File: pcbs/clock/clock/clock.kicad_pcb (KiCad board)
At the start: 2 copper layers, 89 parts, among them J1 USB_B_Micro, Q1 BSS138, Q10 BSS138, Q11 BSS138, Q12 BSS138, Q2 BSS138, Q3 BSS138, Q4 BSS138, Q5 BSS138, Q6 BSS138, Q7 BSS138, Q8 BSS138, Q9 BSS138, SW1 SW_Push, U1 USBLC6-2SC6, U10 KCSC02-105, U11 KCSC02-105, U12 KCSC02-105, U13 KCSC02-105, U14 KCSC02-105, U15 KCSC02-105, U16 KCSC02-105, U2 AP2112K-3.3, U3 SAMD21Exx, U4 PCF85263ATT, U5 TCA6416APWR, U6 AT24CS01-SSHM, U7 KCSC02-105, U8 KCSC02-105, U9 KCSC02-105, Y1 32.768k

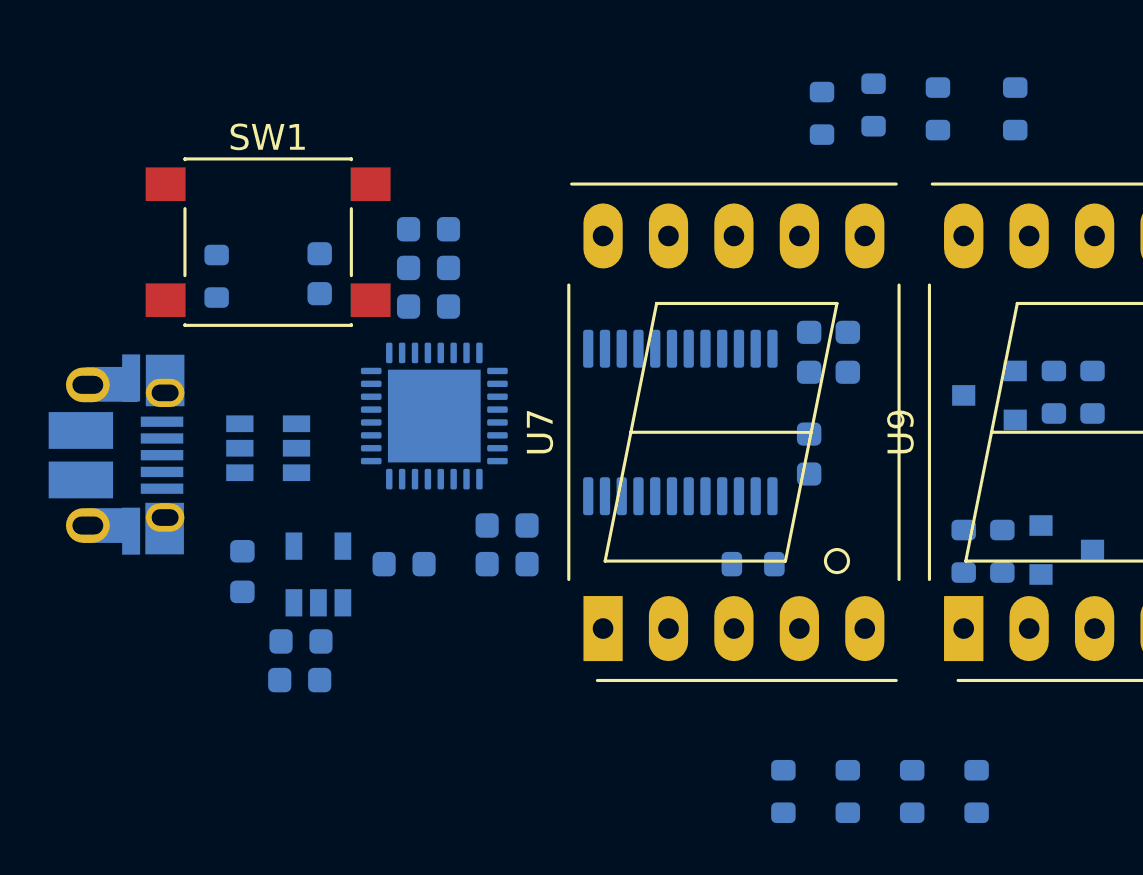
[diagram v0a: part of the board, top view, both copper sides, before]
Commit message: Start clock layout
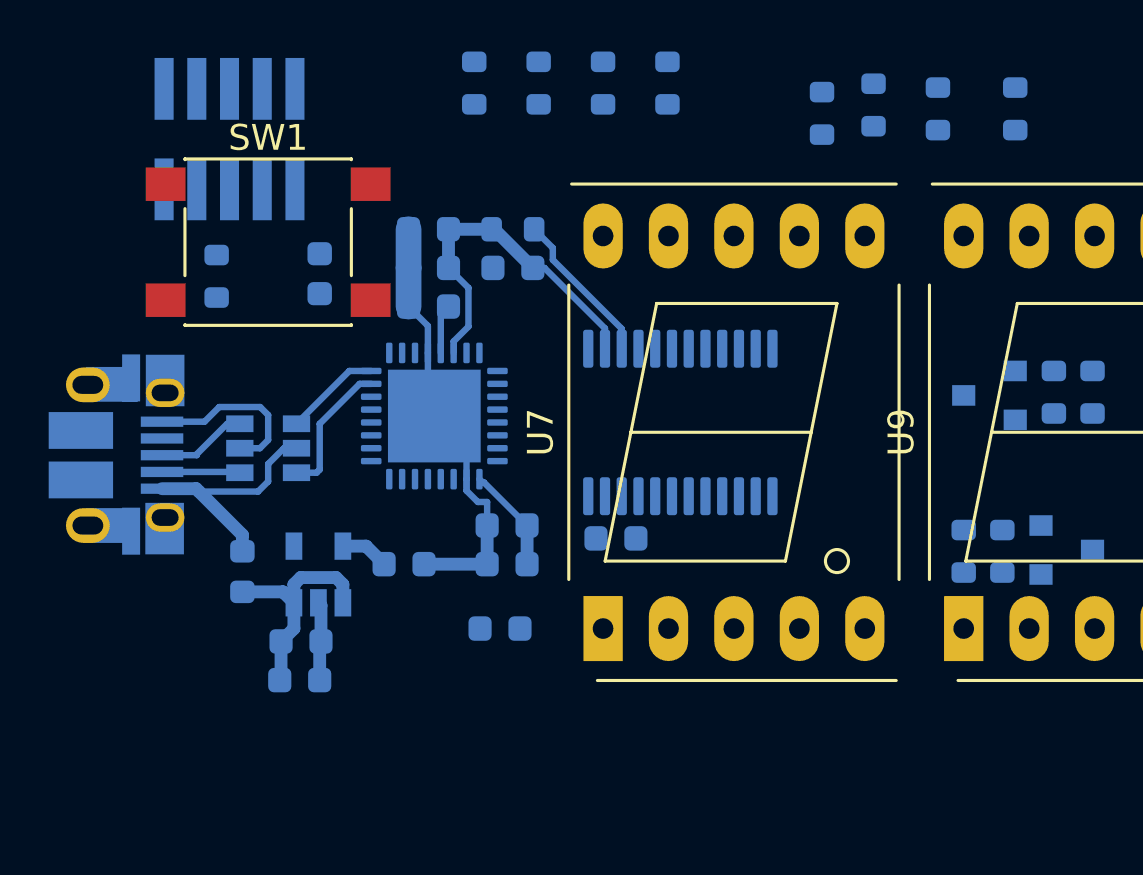
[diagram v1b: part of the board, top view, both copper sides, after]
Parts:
- added J2: CORTEX, Connector_PinHeader_1.27mm:PinHeader_2x05_P1.27mm_Vertical_SMD, B.Cu at (62.5, 116.0)
- moved R11 30.0 mm to (77.0, 113.8)
- moved R12 30.0 mm to (79.5, 113.8)
- moved R13 30.0 mm to (74.5, 113.8)
- moved R16 30.0 mm to (72.0, 113.8)
- moved C12 17.2 mm to (73.0, 135.0), turned to 180 degrees
- moved R8 16.0 mm to (73.5, 119.5), turned to 0 degrees
- moved C11 13.6 mm to (73.5, 121.0), turned to 180 degrees
- moved C13 10.4 mm to (77.5, 131.5), turned to 0 degrees
- turned U5 to 270 degrees
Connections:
- U3 pad 18: /CH6 -> Net-(U3-Pad18)
- U3 pad 19: /CH7 -> Net-(U3-Pad19)
- U3 pad 20: /CH8 -> Net-(U3-Pad20)
- U3 pad 21: /CH9 -> Net-(U3-Pad21)
- U3 pad 22: /CH10 -> Net-(U3-Pad22)
- U3 pad 4: Net-(U3-Pad4) -> /CH6
- U3 pad 5: Net-(U3-Pad5) -> /CH7
- U3 pad 6: Net-(U3-Pad6) -> /CH8
- U3 pad 7: Net-(U3-Pad7) -> /CH9
- U3 pad 8: Net-(U3-Pad8) -> /CH10
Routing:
- net GND: track 0.00 -> 26.7 mm
- net +3V3: track 0.00 -> 19.8 mm
- net Net-(FB1-Pad2): track 0.00 -> 9.38 mm
- net +5V: track 0.00 -> 8.95 mm
- net Net-(R8-Pad2): track 0.00 -> 6.05 mm
- net /USB_N: track 0.00 -> 5.37 mm
- net /USB_P: track 0.00 -> 3.75 mm
- net Net-(J1-Pad3): track 0.00 -> 3.55 mm
- net Net-(J1-Pad2): track 0.00 -> 3.03 mm
- net Net-(C9-Pad2): track 0.00 -> 1.92 mm

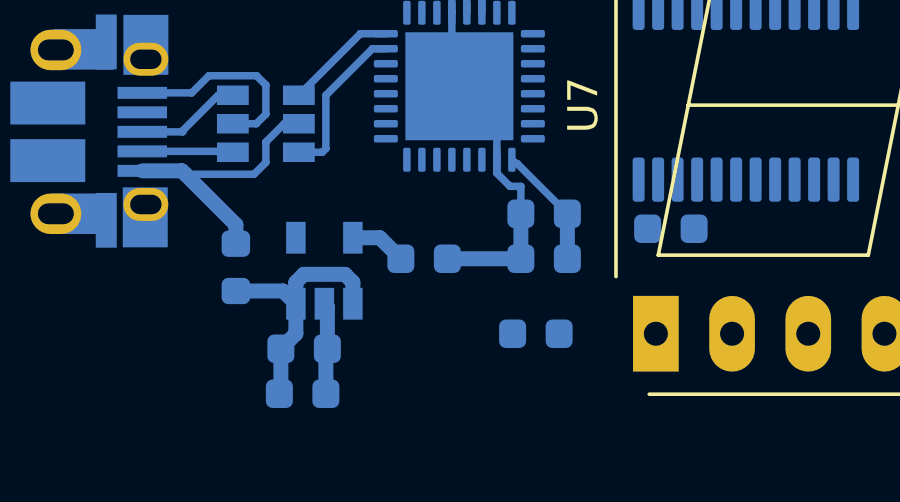
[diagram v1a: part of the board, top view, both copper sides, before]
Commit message: Start clock layout
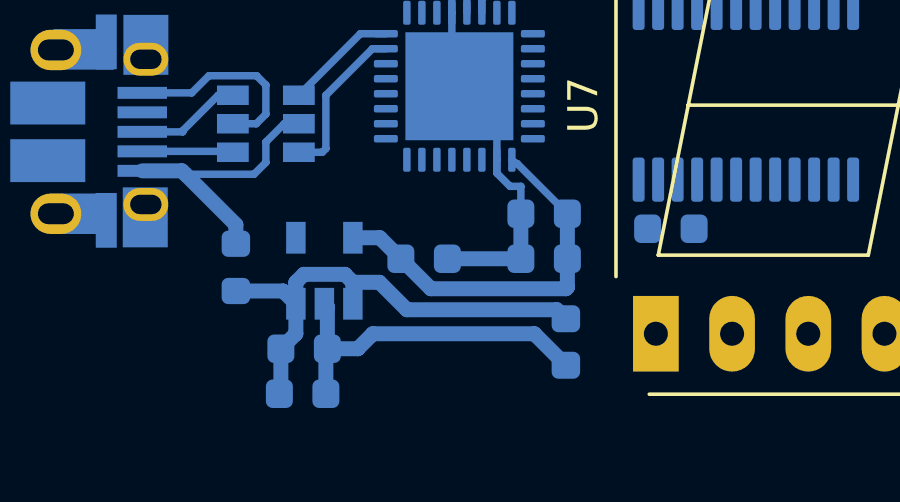
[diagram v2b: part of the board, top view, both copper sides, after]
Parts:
- moved C12 1.04 mm to (74.0, 135.3), turned to 270 degrees
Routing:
- net GND: track 26.7 -> 35.3 mm
- net +5V: track 8.95 -> 16.6 mm
- net +3V3: track 19.8 -> 26.7 mm
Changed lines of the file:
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@@
     (thickness 1.6)
     (drawings 0)
-    (tracks 81)
+    (tracks 93)
     (zones 0)
     (modules 90)
@@
   )
   (module Capacitor_SMD:C_0603_1608Metric (layer B.Cu)
-    (at 73 135 180)
+    (at 74 135.275 270)
     (descr "Capacitor SMD 0603 (1608 Metric), square (rectangular) end terminal, IPC_7351 nominal, (Body size source: IPC-SM-782 page 76, https://www.pcb-3d.com/wordpress/wp-content/uploads/ipc-sm-782a_amendment_1_and_2.pdf), generated with kicad-footprint-generator")
     (tags capacitor)
     (attr smd)
-    (fp_text reference C12 (at 0 1.43) (layer B.SilkS)
+    (fp_text reference C12 (at 0 1.43 90) (layer B.SilkS)
       (effects (font (size 1 1) (thickness 0.15)) (justify mirror))
     )
-    (fp_text value 10u (at 0 -1.43) (layer B.Fab)
+    (fp_text value 10u (at 0 -1.43 90) (layer B.Fab)
       (effects (font (size 1 1) (thickness 0.15)) (justify mirror))
     )
-    (fp_text user %R (at 0 0) (layer B.Fab)
+    (fp_text user %R (at 0 0 90) (layer B.Fab)
       (effects (font (size 0.4 0.4) (thickness 0.06)) (justify mirror))
     )
@@
     (fp_line (start 1.48 0.73) (end 1.48 -0.73) (layer B.CrtYd) (width 0.05))
     (fp_line (start 1.48 -0.73) (end -1.48 -0.73) (layer B.CrtYd) (width 0.05))
-    (pad 2 smd roundrect (at 0.775 0 180) (size 0.9 0.95) (layers B.Cu B.Paste B.Mask) (roundrect_rratio 0.25)
+    (pad 2 smd roundrect (at 0.775 0 270) (size 0.9 0.95) (layers B.Cu B.Paste B.Mask) (roundrect_rratio 0.25)
       (net 2 GND))
-    (pad 1 smd roundrect (at -0.775 0 180) (size 0.9 0.95) (layers B.Cu B.Paste B.Mask) (roundrect_rratio 0.25)
+    (pad 1 smd roundrect (at -0.775 0 270) (size 0.9 0.95) (layers B.Cu B.Paste B.Mask) (roundrect_rratio 0.25)
       (net 5 +5V))
     (model ${KISYS3DMOD}/Capacitor_SMD.3dshapes/C_0603_1608Metric.wrl
@@
   (segment (start 72.5 131) (end 72.5 132.5) (width 0.5) (layer B.Cu) (net 2))
   (segment (start 70.05 132.5) (end 72.5 132.5) (width 0.5) (layer B.Cu) (net 2))
+  (segment (start 72.95 135) (end 74 136.05) (width 0.5) (layer B.Cu) (net 2))
+  (segment (start 67.565002 135) (end 72.95 135) (width 0.5) (layer B.Cu) (net 2))
+  (segment (start 67.065002 135.5) (end 67.565002 135) (width 0.5) (layer B.Cu) (net 2))
+  (segment (start 66.05 135.5) (end 67.065002 135.5) (width 0.5) (layer B.Cu) (net 2))
   (segment (start 71.77501 123.276968) (end 71.77501 121.77501) (width 0.25) (layer B.Cu) (net 3))
   (segment (start 71.77501 121.77501) (end 71 121) (width 0.25) (layer B.Cu) (net 3))
@@
   (segment (start 67.8 131.8) (end 68.5 132.5) (width 0.5) (layer B.Cu) (net 3))
   (segment (start 66.9 131.8) (end 67.8 131.8) (width 0.5) (layer B.Cu) (net 3))
+  (segment (start 74.05 132.5) (end 74.05 133.45) (width 0.5) (layer B.Cu) (net 3))
+  (segment (start 74.05 133.45) (end 74 133.5) (width 0.5) (layer B.Cu) (net 3))
+  (segment (start 69.5 133.5) (end 68.5 132.5) (width 0.5) (layer B.Cu) (net 3))
+  (segment (start 74 133.5) (end 69.5 133.5) (width 0.5) (layer B.Cu) (net 3))
   (segment (start 64.575 133.575) (end 65 134) (width 0.5) (layer B.Cu) (net 5))
   (segment (start 63 133.575) (end 64.575 133.575) (width 0.5) (layer B.Cu) (net 5))
@@
   (segment (start 65 133.284998) (end 65.264999 133.019999) (width 0.5) (layer B.Cu) (net 5))
   (segment (start 65 134) (end 65 133.284998) (width 0.5) (layer B.Cu) (net 5))
+  (segment (start 66.9 133.284998) (end 67.784998 133.284998) (width 0.5) (layer B.Cu) (net 5))
+  (segment (start 67.784998 133.284998) (end 68.70001 134.20001) (width 0.5) (layer B.Cu) (net 5))
+  (segment (start 73.70001 134.20001) (end 74 134.5) (width 0.5) (layer B.Cu) (net 5))
+  (segment (start 68.70001 134.20001) (end 73.70001 134.20001) (width 0.5) (layer B.Cu) (net 5))
   (segment (start 70.7 122.8) (end 71 122.5) (width 0.25) (layer B.Cu) (net 6))
   (segment (start 70.7 124.3) (end 70.7 122.8) (width 0.25) (layer B.Cu) (net 6))

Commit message: Progress
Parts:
- moved C10 133.5 mm to (98.1, 128.7), turned to 180 degrees
- moved U4 129.5 mm to (99.7, 131.2), turned to 180 degrees
- moved Y1 124.4 mm to (104.6, 129.7), turned to 270 degrees
- moved R16 28.2 mm to (86.6, 138.0), turned to 180 degrees
- moved R11 25.0 mm to (83.4, 138.0), turned to 180 degrees
- moved R13 24.3 mm to (77.0, 138.0), turned to 0 degrees
- moved R12 24.2 mm to (80.2, 138.0), turned to 0 degrees
- moved R37 20.0 mm to (94.2, 123.6), turned to 270 degrees
- moved R38 19.2 mm to (95.0, 127.6), turned to 90 degrees
- moved C14 13.9 mm to (95.6, 123.6)
- moved R15 13.1 mm to (77.0, 116.8), turned to 180 degrees
- moved R27 11.3 mm to (106.4, 124.3), turned to 270 degrees
- moved R9 9.83 mm to (83.4, 116.8), turned to 180 degrees
- moved R25 9.11 mm to (104.9, 124.3), turned to 90 degrees
- moved Q7 7.77 mm to (108.9, 124.3), turned to 0 degrees
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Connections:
- U3 pad 13: /CH1 -> /CH6
- U3 pad 14: /CH2 -> /CH7
- U3 pad 15: /CH3 -> /CH8
- U3 pad 16: /CH4 -> /CH9
- U3 pad 17: /CH5 -> /CH10
- U3 pad 4: /CH6 -> /CH1
- U3 pad 5: /CH7 -> /CH2
- U3 pad 6: /CH8 -> /CH3
- U3 pad 7: /CH9 -> /CH4
- U3 pad 8: /CH10 -> /CH5
- U5 pad 10: /Displays/SEG_G -> Net-(U5-Pad10)
- U5 pad 11: /Displays/SEG_DP -> Net-(U5-Pad11)
- U5 pad 17: Net-(U5-Pad17) -> /Displays/SEG_DP
- U5 pad 18: Net-(U5-Pad18) -> /Displays/SEG_C
- U5 pad 19: Net-(U5-Pad19) -> /Displays/SEG_D
- U5 pad 20: Net-(U5-Pad20) -> /Displays/SEG_E
- U5 pad 4: /Displays/SEG_A -> /Displays/SEG_G
- U5 pad 5: /Displays/SEG_B -> /Displays/SEG_F
- U5 pad 6: /Displays/SEG_C -> /Displays/SEG_A
- U5 pad 7: /Displays/SEG_D -> /Displays/SEG_B
- U5 pad 8: /Displays/SEG_E -> Net-(U5-Pad8)
- U5 pad 9: /Displays/SEG_F -> Net-(U5-Pad9)
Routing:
- net GND: track 35.3 -> 328.2 mm, vias 0 -> 6
- net /Displays/SEGE: track 0.00 -> 183.6 mm, vias 0 -> 9
- net /Displays/SEGG: track 0.00 -> 181.5 mm, vias 0 -> 9
- net /Displays/SEGD: track 0.00 -> 177.2 mm, vias 0 -> 9
- net /Displays/SEGF: track 0.00 -> 175.8 mm, vias 0 -> 9
- net /Displays/SEGC: track 0.00 -> 172.1 mm, vias 0 -> 9
- net /Displays/SEGA: track 0.00 -> 171.5 mm, vias 0 -> 9
- net /Displays/SEGDP: track 0.00 -> 165.7 mm
- net /Displays/SEGB: track 0.00 -> 165.0 mm
- net /SCL: track 0.00 -> 49.3 mm, vias 0 -> 2
- net /CH3: track 0.00 -> 42.1 mm
- net /SDA: track 0.00 -> 37.4 mm, vias 0 -> 2
- net Net-(BT1-Pad1): track 0.00 -> 32.8 mm
- net /CLKI: track 0.00 -> 30.8 mm, vias 0 -> 2
- net +3V3: track 26.7 -> 51.3 mm, vias 0 -> 2
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- added copper zone on F.Cu, net GND

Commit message: Progress
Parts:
- moved R31 8.02 mm to (119.3, 123.4)
- moved Q9 7.99 mm to (121.8, 123.2)
- moved R29 7.87 mm to (117.8, 123.4)
- moved R1 3.78 mm to (171.2, 133.7), turned to 90 degrees
- moved R5 3.76 mm to (204.8, 134.2), turned to 90 degrees
- moved R3 3.50 mm to (166.0, 123.8)
- moved R7 3.40 mm to (200.1, 123.8)
- moved Q12 2.10 mm to (224.9, 130.1)
- moved R34 2.10 mm to (220.9, 130.1)
- moved R36 2.10 mm to (222.4, 130.1)
- moved Q2 1.36 mm to (200.7, 134.3)
- moved R6 1.36 mm to (203.2, 134.2)
- moved Q1 0.81 mm to (167.2, 133.9)
- moved R2 0.81 mm to (169.7, 133.7)
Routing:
- net /CH10: track 0.00 -> 182.9 mm, vias 0 -> 4
- net GND: track 328.2 -> 508.6 mm, vias 6 -> 29
- net Net-(BT1-Pad1): track 32.8 -> 207.7 mm, vias 0 -> 2
- net /CH9: track 0.00 -> 165.1 mm, vias 0 -> 4
- net /DT2: track 1.97 -> 165.1 mm, vias 1 -> 4
- net +5V: track 22.7 -> 171.0 mm, vias 0 -> 2
- net /CH8: track 0.00 -> 143.1 mm, vias 0 -> 4
- net /DT1: track 1.04 -> 132.3 mm, vias 1 -> 4
- net /CH7: track 0.00 -> 127.1 mm, vias 0 -> 4
- net /CH6: track 0.00 -> 104.5 mm, vias 0 -> 4
- net /CH5: track 0.00 -> 95.9 mm, vias 0 -> 4
- net /CH4: track 0.00 -> 50.2 mm, vias 0 -> 2
- net +3V3: track 51.3 -> 95.2 mm, vias 2 -> 5
- net /CH3: track 42.1 -> 36.3 mm
- net Net-(Q12-Pad3): track 15.2 -> 20.2 mm
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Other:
- board outline added: 205 x 31.5 mm

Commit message: Beta1
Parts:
- moved BT1 5.50 mm to (242.5, 127.0)
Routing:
- net Net-(BT1-Pad1): track 207.7 -> 178.3 mm
- net GND: track 508.6 -> 510.7 mm
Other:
- board size 205 x 31.5 mm -> 196.7 x 31.5 mm
